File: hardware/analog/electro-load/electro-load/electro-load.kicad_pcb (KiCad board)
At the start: 2 copper layers, 100 x 75 mm, 93 parts, among them J1 AVR-ISP-10, J2 Conn_WallSocket_Earth, J3 INPUT, K1 SANYOU_SRD_Form_C, M1 Noctua NF-A14 5V, Q1 2N2222A, Q2 2N2222A, Q4 IPP055N03L G, Q5 2N2222, SW2 Rotary_Encoder_Switch, U1 ATmega328P-AU, U2 MCP4725A0T-E_CH, U3 LMV321, U4 LMV321, U5 RC1602A, U6 LMV324

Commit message: Added voltage reference REF5020 datasheet
Started work on HW rev 2 of electro load and 5v-from-mains - rev 1 contained misaligned footprints.
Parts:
- removed the C11 at (87.8, 79.8)
- removed the C14 at (56.0, 70.8)
- removed HS1: RS_176-4176, athir:Heatsink_Fischer_SK104-STC-STIC_35x13mm_2xDrill2.5mm
- removed the R19 at (59.5, 73.0)
- removed the R23 at (61.8, 99.2)
- removed the R25 at (52.0, 73.0)
- removed the R27 at (56.0, 73.0)
- removed REF** (x3): MountingHole_2.7mm_M2.5_ISO14580_Pad, MountingHole:MountingHole_2.7mm_M2.5_ISO14580_Pad
- removed the RV5 at (45.5, 95.0)
- removed the TP6 at (57.5, 86.5)
- removed the U4 at (74.5, 61.8)
- added C15: 100n, Capacitor_SMD:C_0603_1608Metric, F.Cu at (38.3, 30.5)
- added C17: 100n, Capacitor_SMD:C_0603_1608Metric, F.Cu at (33.3, 38.5)
- added C18: 100n, Capacitor_SMD:C_0603_1608Metric, F.Cu at (277.1, 78.7)
- added C19: 10u, Capacitor_SMD:C_0603_1608Metric, F.Cu at (270.7, 70.2)
- added C20: 100n, Capacitor_SMD:C_0603_1608Metric, F.Cu at (275.4, 74.7)
- added C21: 100n, Capacitor_SMD:C_0603_1608Metric, F.Cu at (273.2, 70.2)
- added C22: 100n, Capacitor_SMD:C_0603_1608Metric, F.Cu at (277.9, 74.7)
- added C23: 10u, Capacitor_SMD:C_0603_1608Metric, F.Cu at (275.7, 70.7)
- added C24: 10u, Capacitor_SMD:C_0603_1608Metric, F.Cu at (278.2, 70.7)
- added C25: 100n, Capacitor_SMD:C_0603_1608Metric, F.Cu at (72.3, 110.6)
- added C26: 100n, Capacitor_SMD:C_0603_1608Metric, F.Cu at (230.1, 92.8)
- added C9: 100n, Capacitor_SMD:C_0603_1608Metric, F.Cu at (232.2, 96.5)
- added Q3: IPP037N06L3, Package_TO_SOT_THT:TO-220-3_Vertical, F.Cu at (70.0, 58.8)
- added Q6: IPP037N06L3, Package_TO_SOT_THT:TO-220-3_Vertical, F.Cu at (238.0, 133.7)
- added Q7: IPP037N06L3, Package_TO_SOT_THT:TO-220-3_Vertical, F.Cu at (238.0, 64.2)
- added R24: 500m 15W, TestPoint:TestPoint_2Pads_Pitch5.08mm_Drill1.3mm, F.Cu at (44.7, 73.8)
- added R28: 1k, Resistor_SMD:R_0603_1608Metric, F.Cu at (38.3, 34.5)
- added R31: 1k, Resistor_SMD:R_0603_1608Metric, F.Cu at (48.1, 44.4)
- added R34: 100R, Resistor_SMD:R_0603_1608Metric, F.Cu at (40.8, 33.2)
- added R35: 100R, Resistor_SMD:R_0603_1608Metric, F.Cu at (280.4, 36.4)
- added R36: 500m 15W, TestPoint:TestPoint_2Pads_Pitch5.08mm_Drill1.3mm, F.Cu at (57.5, 69.1)
- added R37: 500m 15W, TestPoint:TestPoint_2Pads_Pitch5.08mm_Drill1.3mm, F.Cu at (270.3, 59.7)
- added R38: 1k, Resistor_SMD:R_0603_1608Metric, F.Cu at (280.4, 32.4)
- added R39: 1k, Resistor_SMD:R_0603_1608Metric, F.Cu at (282.9, 37.8)
- added R40: 1k, Resistor_SMD:R_0603_1608Metric, F.Cu at (282.9, 33.8)
- added R41: 1k, Resistor_SMD:R_0603_1608Metric, F.Cu at (48.1, 40.4)
- added R42: 1k, Resistor_SMD:R_0603_1608Metric, F.Cu at (280.4, 28.4)
- added R43: 1k, Resistor_SMD:R_0603_1608Metric, F.Cu at (43.3, 33.2)
- added R44: 1k, Resistor_SMD:R_0603_1608Metric, F.Cu at (282.9, 29.8)
- added R45: 1k, Resistor_SMD:R_0603_1608Metric, F.Cu at (41.3, 25.5)
- added RV8: 6k8 POT, Potentiometer_THT:Potentiometer_Bourns_3296W_Vertical, F.Cu at (278.2, 41.4)
- added RV9: 6k8 POT, Potentiometer_THT:Potentiometer_Bourns_3296W_Vertical, F.Cu at (31.6, 49.5)
- added TP14: TestPoint, athir:testpoint_probe, F.Cu at (51.7, 55.3)
- added TP15: TestPoint, athir:testpoint_probe, F.Cu at (280.8, 24.8)
- added TP16: TestPoint, athir:testpoint_probe, F.Cu at (283.9, 26.2)
- added TP17: TestPoint, athir:testpoint_probe, F.Cu at (280.8, 21.6)
- added TP18: TestPoint, athir:testpoint_probe, F.Cu at (52.3, 52.2)
- added TP9: TestPoint, athir:testpoint_probe, F.Cu at (46.1, 33.6)
- added U10: ADS1115IDGS, Package_SO:TSSOP-10_3x3mm_P0.5mm, F.Cu at (249.5, 83.6)
- added U11: ADS1115IDGS, Package_SO:TSSOP-10_3x3mm_P0.5mm, F.Cu at (271.8, 75.7)
- added U12: LMV321, Package_TO_SOT_SMD:SOT-23-5, F.Cu at (72.3, 106.6)
- added U13: LMV321, Package_TO_SOT_SMD:SOT-23-5, F.Cu at (238.0, 95.6)
- added U5: LMV324, Package_SO:SOIC-14_3.9x8.7mm_P1.27mm, F.Cu at (274.1, 33.8)
- added U7: LMV324, Package_SO:SOIC-14_3.9x8.7mm_P1.27mm, F.Cu at (274.1, 25.3)
- added U8: REF5040ID, Package_SO:SOIC-8_3.9x4.9mm_P1.27mm, F.Cu at (272.7, 83.4)
- added U9: LMV321, Package_TO_SOT_SMD:SOT-23-5, F.Cu at (281.9, 77.2)
- J2: footprint athir:230VAC_PLUG -> athir:Molex-KK-396-5277
- Q4: value IPP055N03L G -> IPP037N06L3
- R20, R21: value 1R 100W -> 100R; footprint TestPoint:TestPoint_2Pads_Pitch5.08mm_Drill1.3mm -> Resistor_SMD:R_0603_1608Metric
- R23: renamed from R18; value 1R 100W -> 500m 15W
- R26: value 100 -> 1k
- RV6: value 2k POT -> 6k8 POT
- SW2: value Rotary_Encoder_Switch -> ROT_ENC; footprint Rotary_Encoder:RotaryEncoder_Alps_EC11E-Switch_Vertical_H20mm -> Connector_PinHeader_2.54mm:PinHeader_1x05_P2.54mm_Vertical
- U3: value LMV321 -> LMV324; footprint Package_TO_SOT_SMD:SOT-23-5 -> Package_SO:SOIC-14_3.9x8.7mm_P1.27mm
- moved U3 187.5 mm to (261.7, 45.0), turned to 90 degrees
- moved Q2 169.4 mm to (239.4, 102.7), turned to 90 degrees
- moved R11 166.8 mm to (238.1, 92.2), turned to 0 degrees
- moved RV4 163.3 mm to (237.8, 82.7), turned to 90 degrees
- moved R9 161.8 mm to (234.3, 96.5), turned to 90 degrees
- moved R12 155.1 mm to (232.2, 92.8), turned to 90 degrees
- moved R13 154.7 mm to (234.3, 92.8), turned to 90 degrees
- moved RV3 150.3 mm to (232.0, 87.8), turned to 270 degrees
- moved R10 143.6 mm to (230.1, 96.5), turned to 270 degrees
- moved J1 96.2 mm to (198.0, 60.8), turned to 0 degrees
- moved Q4 85.3 mm to (49.7, 128.1), turned to 270 degrees
- moved R21 84.7 mm to (33.3, 30.5)
- moved J3 75.6 mm to (168.1, 32.3), turned to 180 degrees
- moved R20 71.2 mm to (40.8, 37.2)
- moved J2 68.9 mm to (200.8, 78.6), turned to 0 degrees
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- renumbered C12 to C10, C13 to C11, C18 to C12, C19 to C13, C20 to C14, C15 to C16, C10 to C8, D6 to D1, D7 to D2, R33 to R15, R34 to R16, R35 to R17, R16 to R18, R17 to R19, R24 to R25, R29 to R27, R30 to R29, R28 to R30, R31 to R33, RV7 to RV5, RV8 to RV7, TP13 to TP12, TP12 to TP13, TP7 to TP6, TP8 to TP7, TP9 to TP8, U5 to U4
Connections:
- net Net-(K1-Pad1) renamed /Current Measurements/LOAD_CURRENT
- D2 pad 1: Net-(D7-Pad1) -> Net-(D2-Pad1)
- K1 pad 4: (no net) -> Net-(K1-Pad4)
- Q4 pad 1: Net-(Q3-Pad1) -> Net-(Q4-Pad1)
- Q4 pad 3: Net-(Q3-Pad3) -> Net-(Q4-Pad3)
- R13 pad 1: /TEMP_0 -> /Temperature Control/TEMP_0
- R15 pad 1: Net-(R33-Pad1) -> Net-(R15-Pad1)
- R16 pad 1: Net-(R34-Pad1) -> Net-(R16-Pad1)
- R17 pad 2: Net-(R35-Pad2) -> Net-(R17-Pad2)
- R20 pad 1: Net-(Q3-Pad3) -> Net-(R20-Pad1)
- R20 pad 2: GND -> Net-(Q3-Pad1)
- R21 pad 1: Net-(Q3-Pad3) -> Net-(R21-Pad1)
- R21 pad 2: GND -> Net-(Q4-Pad1)
- R26 pad 1: Net-(C14-Pad2) -> Net-(Q3-Pad3)
- R26 pad 2: Net-(Q3-Pad1) -> Net-(R26-Pad2)
- R27 pad 1: Net-(Q3-Pad3) -> Net-(Q4-Pad3)
- R30 pad 1: Net-(D7-Pad1) -> Net-(D2-Pad1)
- R32 pad 2: /CUR_MEAS -> /Current Measurements/CUR_MEAS_1
- R33 pad 1: Net-(R31-Pad1) -> Net-(R33-Pad1)
- R33 pad 2: /V_MEAS -> /Current Measurements/V_MEAS
- R8 pad 1: /TEMP_1 -> /Temperature Control/TEMP_1
- RV5 pad 2: Net-(D7-Pad1) -> Net-(D2-Pad1)
- RV6 pad 1: Net-(Q3-Pad3) -> Net-(R28-Pad2)
- RV6 pad 2: Net-(R25-Pad2) -> Net-(R31-Pad1)
- TP10 pad 1: Net-(D7-Pad1) -> Net-(D2-Pad1)
- TP11 pad 1: Net-(C14-Pad2) -> /Current Measurements/CUR_MEAS_0
- TP12 pad 1: /CUR_MEAS -> /Current Measurements/CUR_MEAS_1
- TP13 pad 1: /V_MEAS -> /Current Measurements/V_MEAS
- TP8 pad 1: Net-(TP9-Pad1) -> Net-(Q3-Pad3)
- U1 pad 23: /CUR_MEAS -> /ADC_0_ALERT
- U1 pad 24: /V_MEAS -> /ADC_1_ALERT
- U1 pad 25: /TEMP_1 -> (no net)
- U1 pad 26: /TEMP_0 -> (no net)
- U3 pad 1: Net-(R5-Pad2) -> Net-(R20-Pad1)
- U3 pad 2: GND -> Net-(Q3-Pad3)
- U3 pad 3: Net-(R6-Pad1) -> /Current Measurements/CURRENT_SET
- U3 pad 4: Net-(R7-Pad1) -> +5V
- U3 pad 5: +5V -> Net-(R26-Pad2)
- U6 pad 1: Net-(C14-Pad2) -> Net-(R34-Pad1)
- U6 pad 13: Net-(TP9-Pad1) -> Net-(R43-Pad2)
- U6 pad 14: Net-(TP9-Pad1) -> Net-(R45-Pad1)
- U6 pad 2: Net-(R25-Pad2) -> Net-(Q6-Pad3)
- U6 pad 3: Net-(TP9-Pad1) -> /Current Measurements/CURRENT_SET
- U6 pad 5: Net-(D7-Pad1) -> (no net)
- U6 pad 6: Net-(R31-Pad1) -> (no net)
- U6 pad 7: Net-(R31-Pad1) -> (no net)
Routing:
- net Net-(Q3-Pad3): track 167.2 -> 0.00 mm, vias 1 -> 0
- net /Current Measurements/LOAD_CURRENT: track 64.2 -> 0.00 mm
- net Net-(R25-Pad2): track 55.2 -> 0.00 mm
- net /TEMP_0: track 37.7 -> 0.00 mm, vias 2 -> 0
- net (no net): track 0.00 -> 37.7 mm, vias 0 -> 2
- net /MISO: track 33.0 -> 0.00 mm, vias 3 -> 0
- net /SCK: track 31.8 -> 0.00 mm, vias 3 -> 0
- net /MOSI: track 30.7 -> 0.00 mm, vias 2 -> 0
- net Net-(Q1-Pad2): track 29.2 -> 0.00 mm, vias 2 -> 0
- net Net-(R41-Pad2): track 41.4 -> 14.1 mm
- net /CUR_SET: track 26.4 -> 0.00 mm
- net Net-(C14-Pad2): track 23.5 -> 0.00 mm, vias 2 -> 0
- net +5V: track 480.3 -> 457.6 mm, vias 25 -> 26
- net /FAN_RPM: track 23.5 -> 42.4 mm
- net Net-(R33-Pad1): track 18.9 -> 0.00 mm
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- added copper zone on B.Cu, net /Current Measurements/LOAD_CURRENT
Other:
- board size 100 x 75 mm -> 175 x 119 mm
- board text added: "Electro-Load Rev 2 2016"
- board text removed: "Electro-Load 8A @ +30V Rev 1 2014"

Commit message: Arranged mosfets and temperature probes to amplifier casing.
Added Power schematic from 5v-from-mains
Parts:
- moved R24 187.1 mm to (220.5, 137.8)
- moved TP16 91.1 mm to (210.9, 80.7)
- moved R38 91.1 mm to (207.4, 86.9)
- moved R40 91.1 mm to (209.9, 88.3)
- moved R35 91.1 mm to (207.4, 90.9)
- moved R39 91.1 mm to (209.9, 92.3)
- moved R42 91.1 mm to (207.4, 82.9)
- moved R44 91.1 mm to (209.9, 84.3)
- moved TP15 91.1 mm to (207.8, 79.3)
- moved TP17 91.1 mm to (207.8, 76.1)
- moved U3 91.1 mm to (188.7, 99.5)
- moved U5 91.1 mm to (201.1, 88.3)
- moved U7 91.1 mm to (201.1, 79.8)
- moved C10 79.0 mm to (78.2, 105.0)
- moved RV2 79.0 mm to (64.7, 80.2), turned to 90 degrees
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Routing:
- net +5V: track 457.6 -> 91.9 mm, vias 26 -> 6
- net /V_MEAS: track 76.3 -> 8.68 mm, vias 4 -> 2
- net /SDA: track 73.2 -> 6.21 mm, vias 4 -> 0
- net /SCL: track 70.8 -> 13.9 mm, vias 4 -> 2
- net /RELAY_EN: track 61.2 -> 4.50 mm, vias 2 -> 0
- net /ROT_B: track 60.0 -> 9.57 mm, vias 8 -> 2
- net /CUR_MEAS: track 78.7 -> 28.9 mm, vias 4 -> 2
- net /TEMP_1: track 39.4 -> 0.00 mm, vias 4 -> 0
- net /ROT_SW: track 47.3 -> 13.8 mm
- net Net-(R6-Pad1): track 30.6 -> 0.00 mm
- net /FAN_RPM: track 42.4 -> 16.5 mm
- net Net-(R7-Pad2): track 20.3 -> 0.00 mm
- net Net-(R5-Pad2): track 17.6 -> 0.00 mm
- net /FAN_PWM: track 32.1 -> 15.7 mm
- net /Current Measurements/CUR_MEAS_1: track 0.00 -> 16.1 mm, vias 0 -> 2
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- removed copper zone on B.Cu, net /Current Measurements/LOAD_CURRENT
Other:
- board size 175 x 119 mm -> 180 x 119 mm

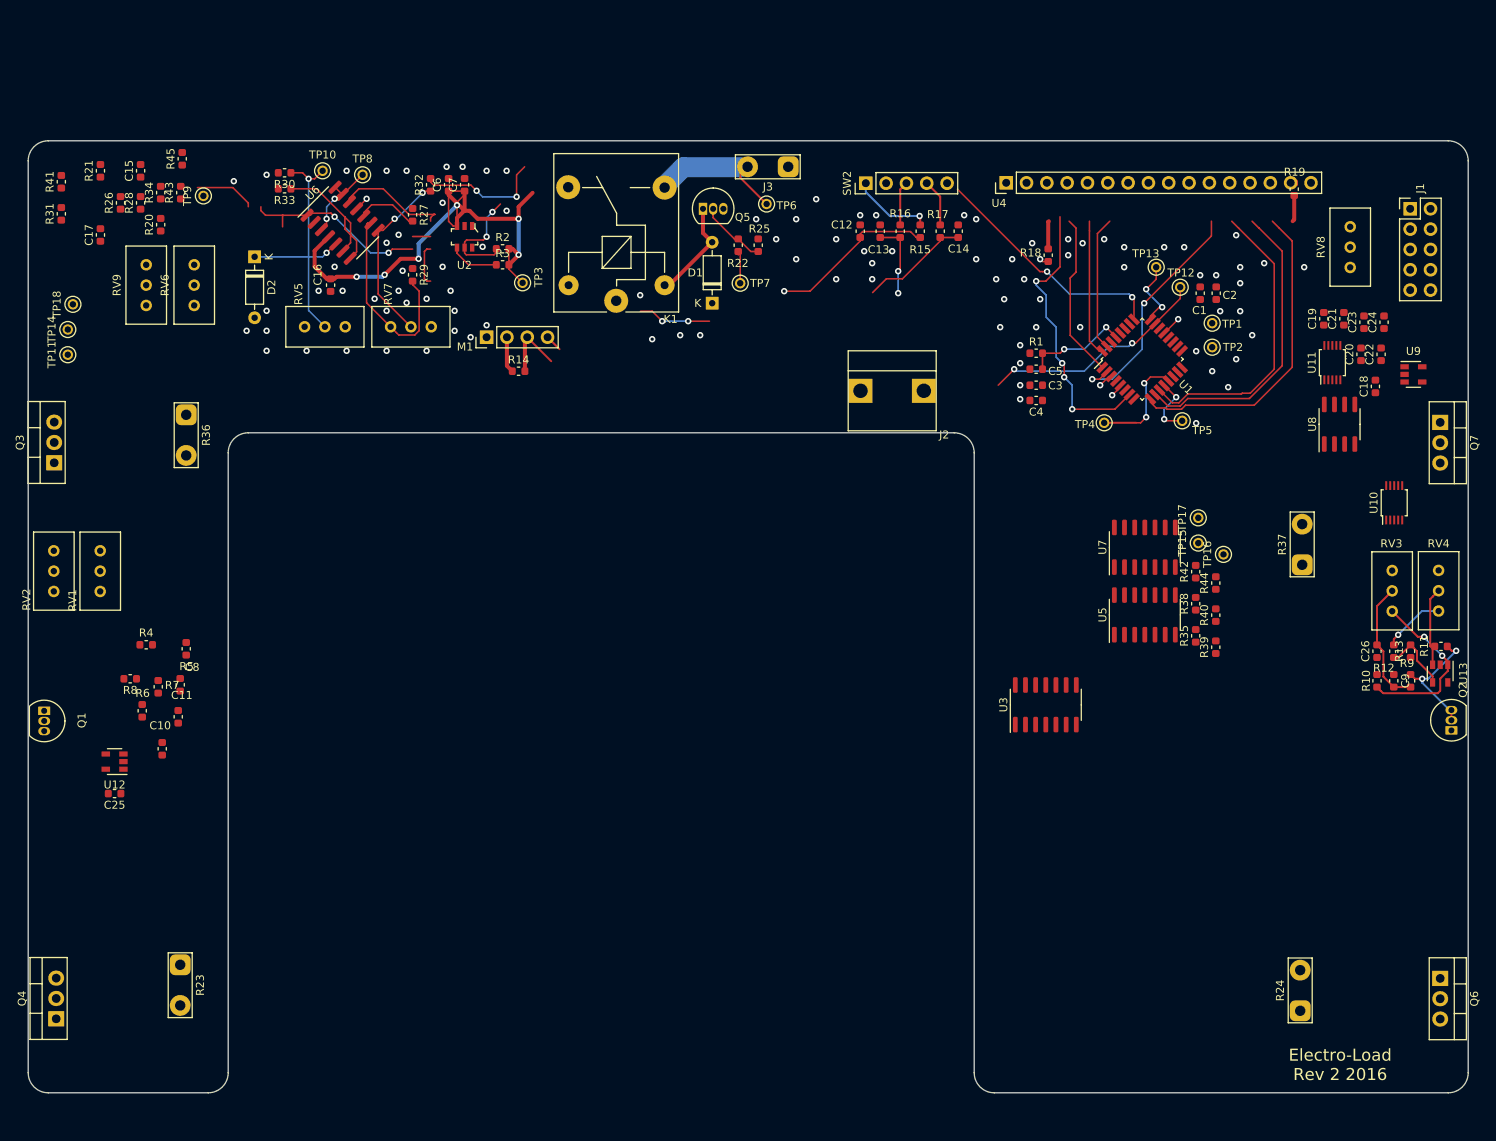
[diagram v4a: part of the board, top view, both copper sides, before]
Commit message: Added basic 3D model of amplifier encasing
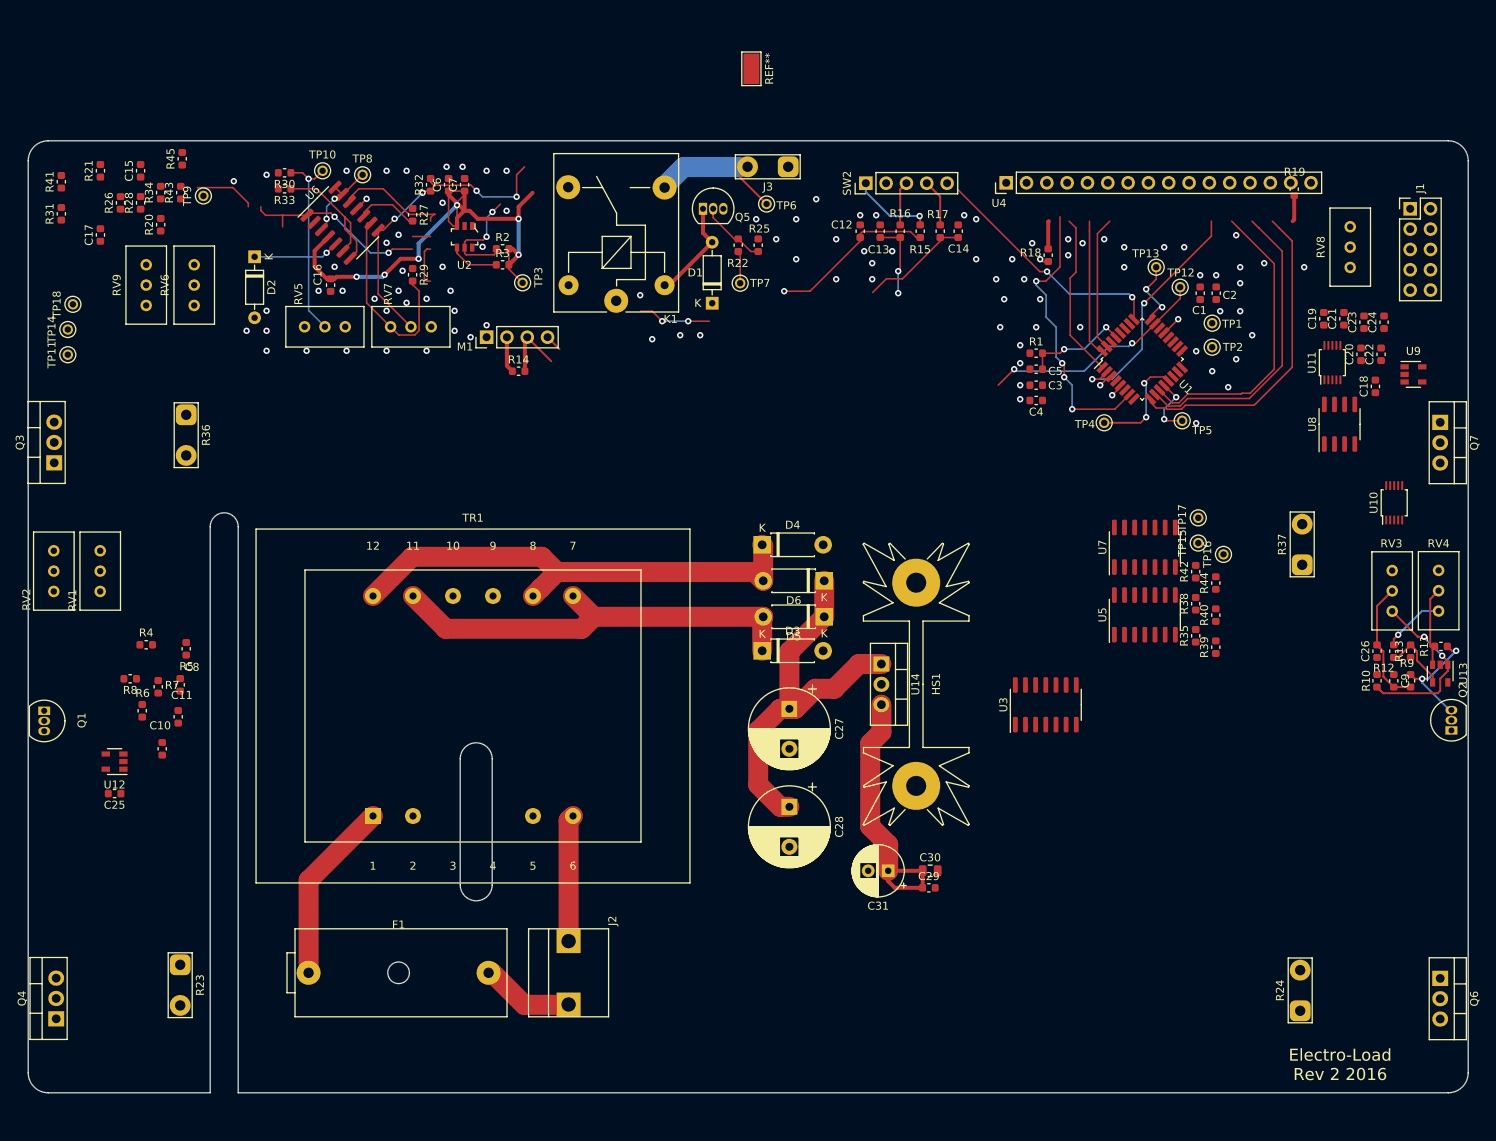
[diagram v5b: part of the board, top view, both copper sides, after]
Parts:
- added C27: 1000u, Capacitor_THT:CP_Radial_D10.0mm_P5.00mm, F.Cu at (156.7, 100.0)
- added C28: 1000u, Capacitor_THT:CP_Radial_D10.0mm_P5.00mm, F.Cu at (156.7, 112.2)
- added C29: 100n, Capacitor_SMD:C_0603_1608Metric, F.Cu at (174.1, 122.4)
- added C30: 10u, Capacitor_SMD:C_0805_2012Metric, F.Cu at (174.2, 120.2)
- added C31: 10u, Capacitor_THT:CP_Radial_D6.3mm_P2.50mm, F.Cu at (169.0, 120.2)
- added D3: 1N5819, Diode_THT:D_DO-41_SOD81_P7.62mm_Horizontal, F.Cu at (153.2, 92.8)
- added D4: 1N5819, Diode_THT:D_DO-41_SOD81_P7.62mm_Horizontal, F.Cu at (153.2, 79.5)
- added D5: 1N5819, Diode_THT:D_DO-41_SOD81_P7.62mm_Horizontal, F.Cu at (161.0, 88.5)
- added D6: 1N5819, Diode_THT:D_DO-41_SOD81_P7.62mm_Horizontal, F.Cu at (161.0, 84.0)
- added F1: 500mA, athir:KK-Fuseholder, F.Cu at (107.8, 133.0)
- added HS1: Heatsink, athir:Heatsink_Fischer_SK104-STC-STIC_35x13mm_2xDrill2.5mm, F.Cu at (172.5, 96.9)
- added REF**: TestPoint_Keystone_5019_Minature, TestPoint:TestPoint_Keystone_5019_Minature, F.Cu at (151.9, 20.0)
- added TR1: Transformer_1P_2S, Transformer_THT:Transformer_Breve_TEZ-44x52, F.Cu at (104.6, 113.4)
- added U14: LM7805_TO220, Package_TO_SOT_THT:TO-220-3_Vertical, F.Cu at (168.2, 94.4)
- moved J2 83.2 mm to (129.1, 133.0), turned to 90 degrees
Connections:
- J2 pad 1: +5V -> Net-(F1-Pad2)
- J2 pad 2: GND -> Net-(J2-Pad2)
- K1 pad 4: Net-(K1-Pad4) -> (no net)
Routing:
- net Net-(D4-Pad1): track 0.00 -> 60.8 mm
- net Net-(D3-Pad1): track 0.00 -> 54.1 mm
- net Net-(C27-Pad1): track 0.00 -> 48.4 mm
- net +5V: track 91.9 -> 126.6 mm
- net Net-(F1-Pad1): track 0.00 -> 22.9 mm
- net Net-(J2-Pad2): track 0.00 -> 15.9 mm
- net Net-(F1-Pad2): track 0.00 -> 11.7 mm
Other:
- outline, holes or cut-outs redrawn
